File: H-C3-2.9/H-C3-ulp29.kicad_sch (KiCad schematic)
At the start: 54 parts, among them CN1 HX JN1.27-2X5 TP H4.9, J1 USB_C_Receptacle_USB2.0, J2 AFC24-S24FIC-00, J4 SM04B-SRSS-TB_LF__SN_, Q1 Si1308, Q2 Si2301CDS, SW1 TM-2023, SW3 K2-1806SQ-A2DW-04, U1 E73-2G4M08S1C, U2 MCP1700-3302E_SOT23, U8 PCF8563T, Y1 Crystal_Small, Y2 RTC_Crystal_32MHz

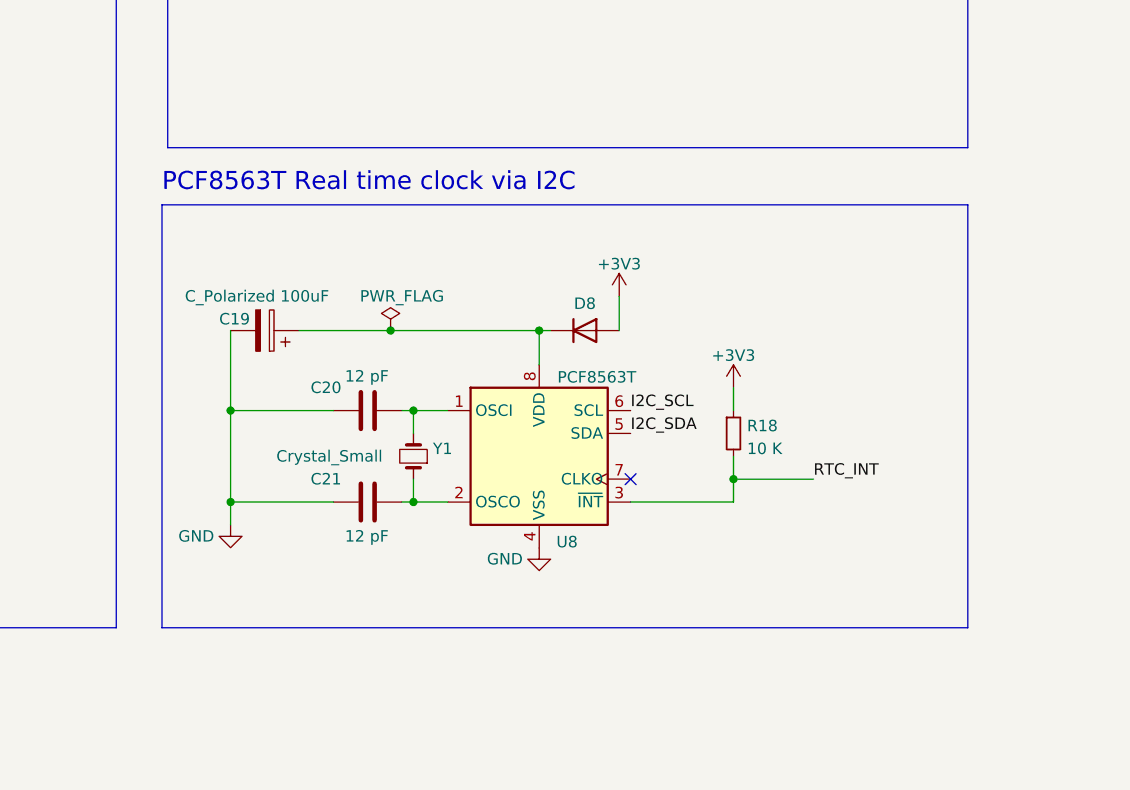
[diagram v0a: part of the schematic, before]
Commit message: RTC is out, use internal one
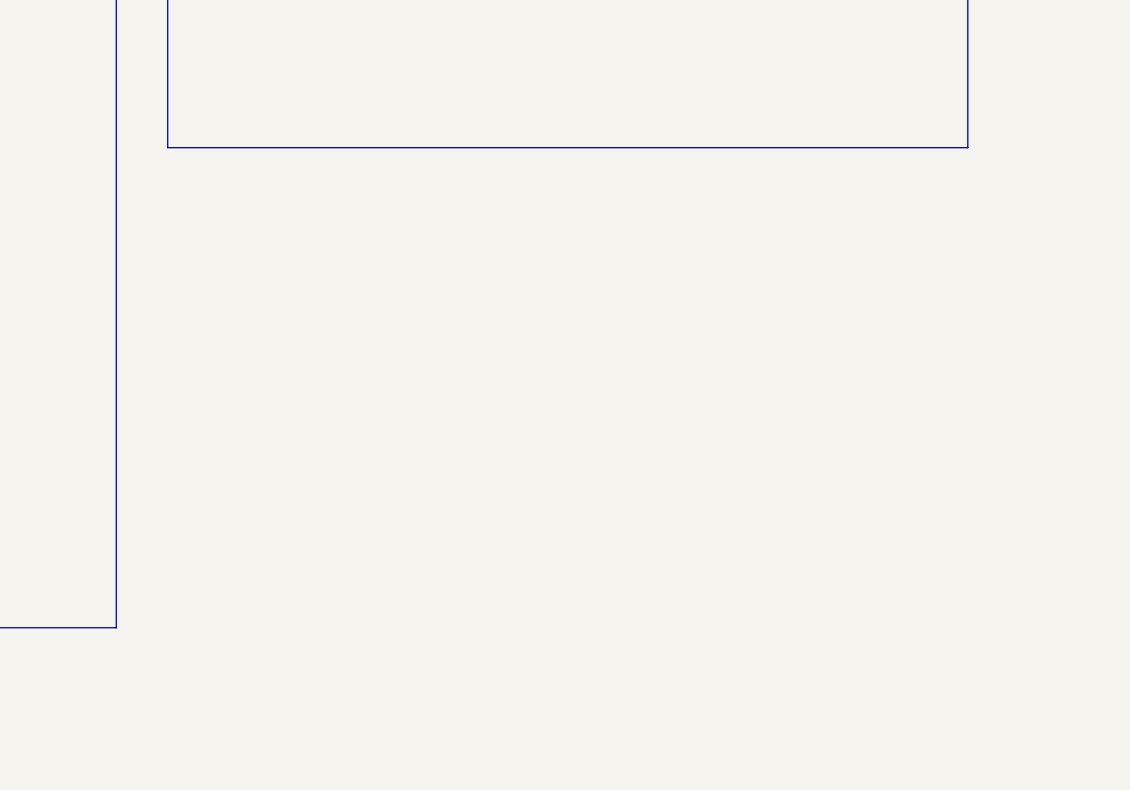
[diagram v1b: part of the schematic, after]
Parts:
- removed C19: C_Polarized 100uF, Capacitor_Tantalum_SMD:CP_EIA-3528-21_Kemet-B, symbol Device:C_Polarized
- removed C20, C21: 12 pF, Capacitor_SMD:C_0603_1608Metric, symbol Device:C
- removed D8: 1N4148WS, Diode_SMD:D_SOD-323, symbol Diode:1N4148WS
- removed R18: 10 K, Resistor_SMD:R_0603_1608Metric, symbol Device:R_Small
- removed U8: PCF8563T, Package_SO:SOIC-8_3.9x4.9mm_P1.27mm, symbol Timer_RTC:PCF8563T
- removed Y1: Crystal_Small, footprints:Q13FC1350000400-Crystal, symbol Device:Crystal_Small
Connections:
- no-connect marks 12 -> 11
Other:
- note removed: "PCF8563T Real time clock via I2C"

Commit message: 1.0 schematics needs last feedback
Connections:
- net SW0: now also U1.42 (P1.06)
- no-connect marks 11 -> 19
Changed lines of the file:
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@@
+	)
+	(no_connect
+		(at 130.81 78.74)
+	)
+	(no_connect
+		(at 130.81 76.2)
 	)
 	(no_connect
@@
 	)
 	(no_connect
+		(at 151.13 96.52)
+	)
+	(no_connect
+		(at 171.45 96.52)
+	)
+	(no_connect
 		(at 257.175 77.47)
 	)
@@
 	)
 	(no_connect
+		(at 130.81 66.04)
+	)
+	(no_connect
 		(at 190.5 52.07)
 	)
@@
 	(no_connect
 		(at 269.24 158.75)
+	)
+	(no_connect
+		(at 158.75 96.52)
+	)
+	(no_connect
+		(at 130.81 81.28)
+	)
+	(no_connect
+		(at 176.53 96.52)
 	)
 	(no_connect
@@
 				(hide yes)
 			)
+		)
+	)
+	(global_label "SW0"
+		(shape input)
+		(at 190.5 49.53 0)
+		(fields_autoplaced yes)
+		(effects
+			(font
+				(size 1.27 1.27)
+			)
+			(justify left)
+		)
+		(property "Intersheetrefs" "${INTERSHEET_REFS}"
+			(at 197.3556 49.53 0)
+			(effects
+				(font
+					(size 1.27 1.27)
+				)
+				(justify left)
+				(hide yes)
+			)

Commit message: Pre-release please check routing
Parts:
- added R6, R9: 470k, Resistor_SMD:R_0402_1005Metric, symbol Device:R
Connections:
- net GND: now also R9.2
- net +VBAT: now reaches BT1.1 (+), Q2.3 (D)
- net +VBAT: now also R6.1
- net at U1.7 (AI0): now also R6.2, R9.1
- net SWO ??: no longer names the net of CN1.5
- no-connect marks 19 -> 20
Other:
- note added: "Battery measure"
- note added: "DOWN"
- note added: "SELECT"
- note added: "UP"

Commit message: FAB attempt 1
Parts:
- added J3: Conn_01x07, Connector_PinHeader_2.54mm:PinHeader_1x07_P2.54mm_Vertical, symbol Connector_Generic:Conn_01x07
- CN1: LCSC (none) -> C42372555; LCSC Part C42372555 -> (none)
- D5: LCSC C8598 -> C8598
- R10: LCSC C25804 -> C25744
- R21, R3, R7: LCSC C4322213 -> C25744
- SW1: LCSC (none) -> C318951; LCSC Part C318951 -> (none)
- SW3: LCSC (none) -> C19100323; LCSC Part C19100323 -> (none)
- TP1, TP2, TP3: now left out of the parts list
- U1: LCSC (none) -> C356849; LCSC Part C356849 -> (none)
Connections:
- net +3V3: now also J3.6 (Pin_6)
- net GND: now also J3.7 (Pin_7)
- net P0.26: now reaches U1.12 (P0.26)
- net P0.26: now also J3.4 (Pin_4)
- net P0.20: now reaches U1.32 (P0.20)
- net P0.20: now also J3.3 (Pin_3)
- net P0.13: now reaches U1.33 (P0.13)
- net P0.13: now also J3.5 (Pin_5)
- net P0.22: now reaches U1.34 (P0.22)
- net P0.22: now also J3.2 (Pin_2)
- net P1.00: now reaches U1.36 (P1.00)
- net P1.00: now also J3.1 (Pin_1)
- no-connect marks 20 -> 22
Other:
- note added: "Ebyte nRF52840 BLE5.0 MCU"
- note added: "Extra IO headers"
- note removed: "Ebyte nRF52832 BLE5.0 MCU"

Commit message: Updated for 1.1
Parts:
- added C18: C_Pol 100uF, footprints:C7171_CAP, symbol Device:C_Polarized
- added C3, C4: 15pF, Capacitor_SMD:C_0402_1005Metric, symbol Device:C
- added C5: 100nF, Capacitor_SMD:C_0402_1005Metric, symbol Device:C
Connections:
- net +3V3: now also C18.1, C5.2
- net GND: now also C18.2, C3.1, C4.1, C5.1
- net SW0: now also SW1.T; no longer SW1.C
- net at R2.2: now also SW1.C; no longer SW1.T
- net at U1.13 (XL2), Y2.1: now also C4.2
- net at U1.11 (XL1), Y2.2: now also C3.2
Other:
- moved on the sheet: R2
